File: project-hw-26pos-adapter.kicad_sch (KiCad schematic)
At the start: 3 parts, among them J1 SM04B-SRSS-TB(LF)(SN), J2 3220-26-0300-00, U1 Pink Panda v2.1.0

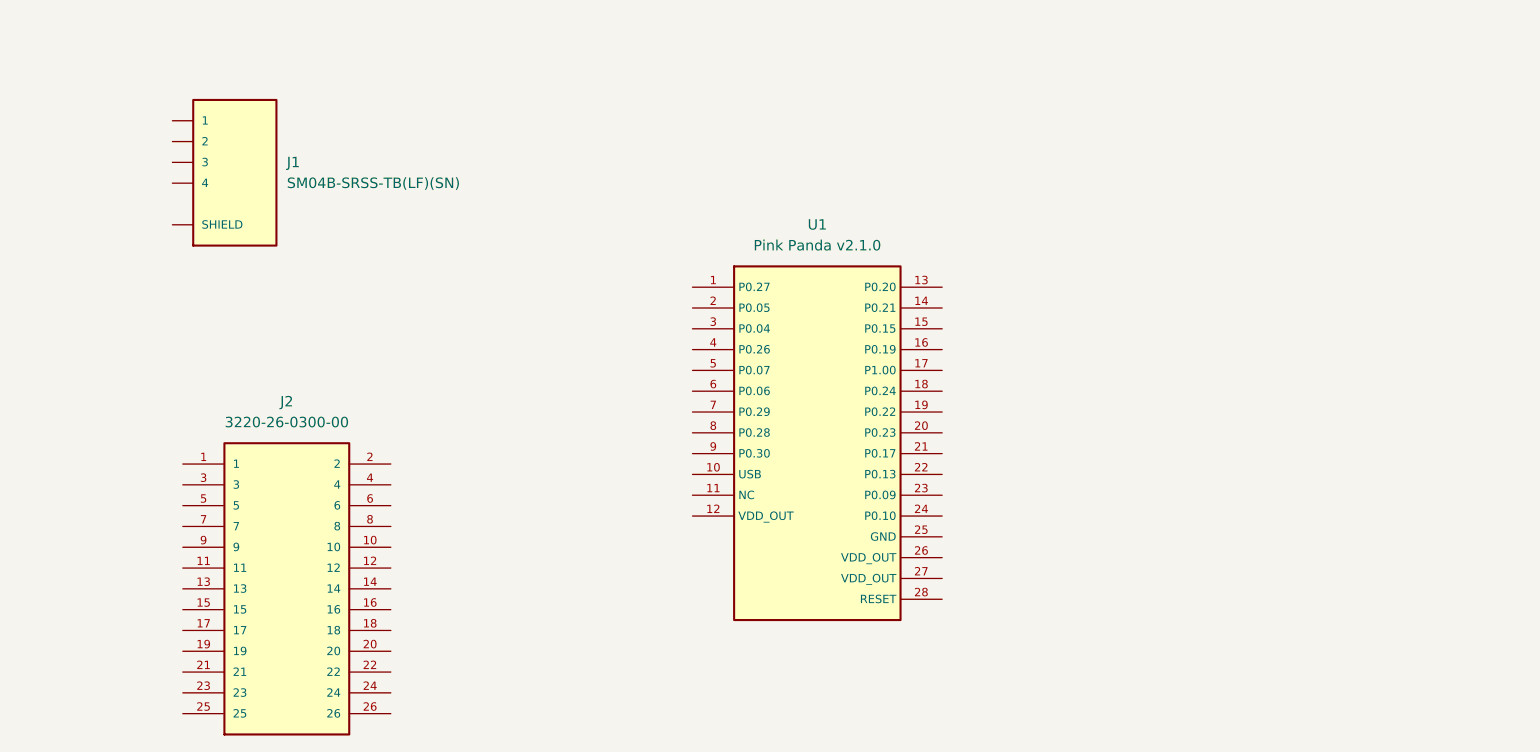
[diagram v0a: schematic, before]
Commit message: sch: add connections
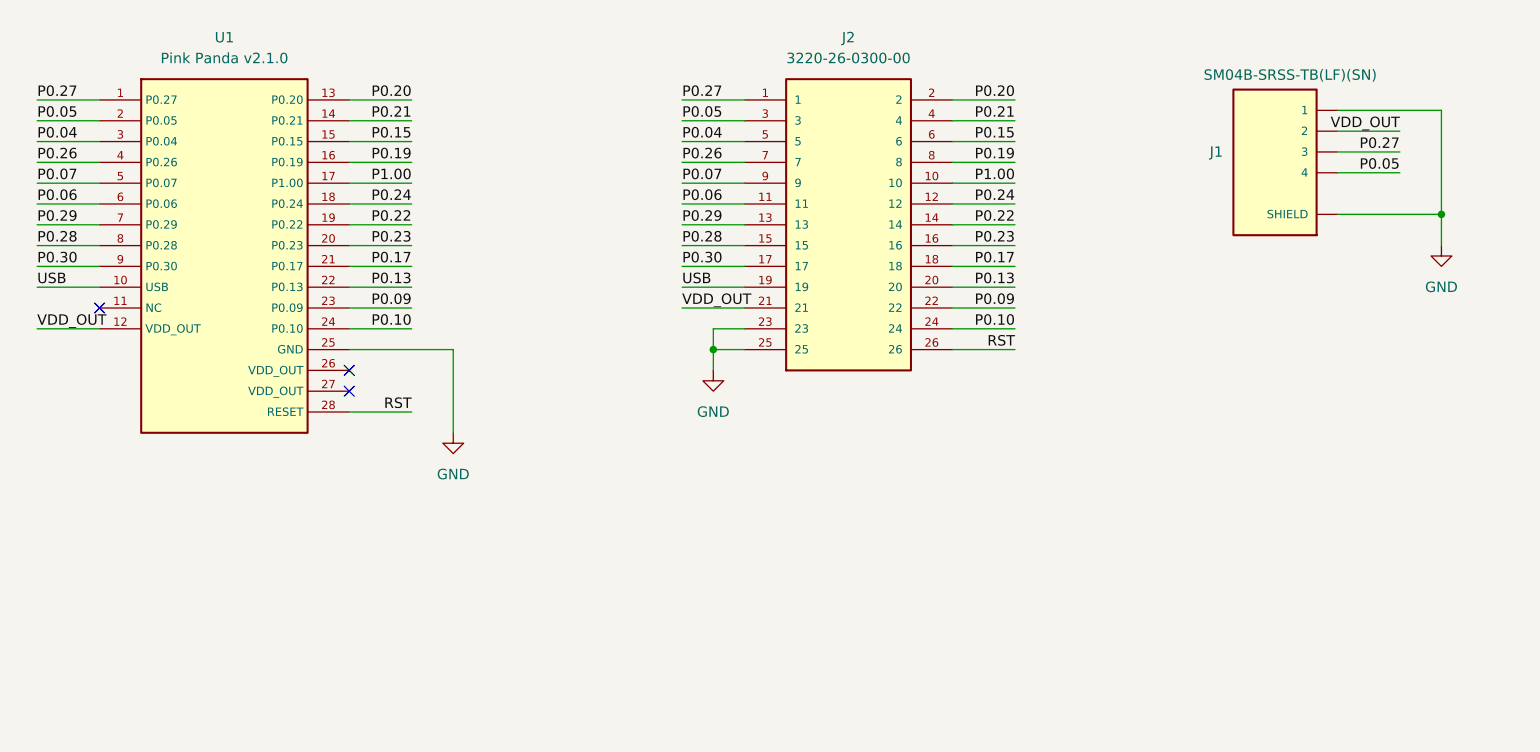
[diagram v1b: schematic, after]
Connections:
- net P0.27: now reaches U1.1 (P0.27)
- net P0.27: now also J1.3, J2.1
- net USB: now reaches U1.10 (USB)
- net USB: now also J2.19
- net VDD_OUT: now reaches U1.12 (VDD_OUT)
- net VDD_OUT: now also J1.2, J2.21
- net P0.20: now reaches U1.13 (P0.20)
- net P0.20: now also J2.2
- net P0.21: now reaches U1.14 (P0.21)
- net P0.21: now also J2.4
- net P0.15: now reaches U1.15 (P0.15)
- net P0.15: now also J2.6
- net P0.19: now reaches U1.16 (P0.19)
- net P0.19: now also J2.8
- net P1.00: now reaches U1.17 (P1.00)
- net P1.00: now also J2.10
- net P0.24: now reaches U1.18 (P0.24)
- net P0.24: now also J2.12
- net P0.22: now reaches U1.19 (P0.22)
- net P0.22: now also J2.14
- net P0.05: now reaches U1.2 (P0.05)
- net P0.05: now also J1.4, J2.3
- net P0.23: now reaches U1.20 (P0.23)
- net P0.23: now also J2.16
- net P0.17: now reaches U1.21 (P0.17)
- net P0.17: now also J2.18
- net P0.13: now reaches U1.22 (P0.13)
- net P0.13: now also J2.20
- net P0.09: now reaches U1.23 (P0.09)
- net P0.09: now also J2.22
- net P0.10: now reaches U1.24 (P0.10)
- net P0.10: now also J2.24
- net GND: now reaches U1.25 (GND)
- net GND: now also J1.1, J1.S1 (SHIELD), J1.S2 (SHIELD), J2.23, J2.25
- net RST: now reaches U1.28 (RESET)
- net RST: now also J2.26
- net P0.04: now reaches U1.3 (P0.04)
- net P0.04: now also J2.5
- net P0.26: now reaches U1.4 (P0.26)
- net P0.26: now also J2.7
- net P0.07: now reaches U1.5 (P0.07)
- net P0.07: now also J2.9
- net P0.06: now reaches U1.6 (P0.06)
- net P0.06: now also J2.11
- net P0.29: now reaches U1.7 (P0.29)
- net P0.29: now also J2.13
- net P0.28: now reaches U1.8 (P0.28)
- net P0.28: now also J2.15
- net P0.30: now reaches U1.9 (P0.30)
- net P0.30: now also J2.17
- no-connect marks 0 -> 3
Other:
- moved on the sheet: J1, J2, U1

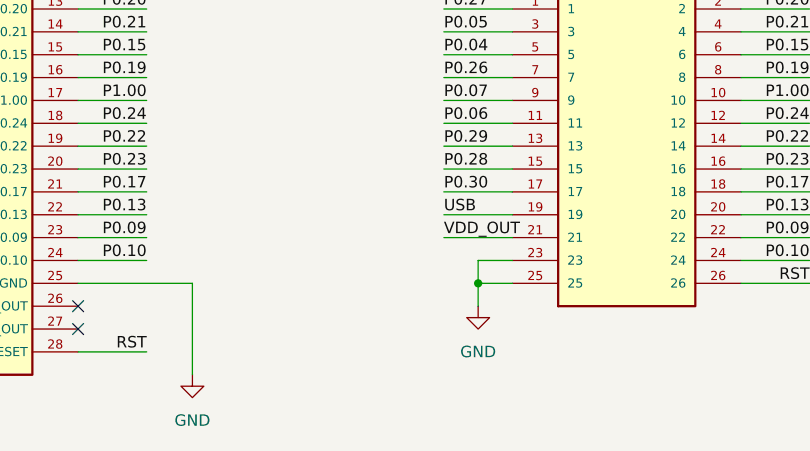
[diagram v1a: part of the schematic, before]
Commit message: pcb: first rough routing
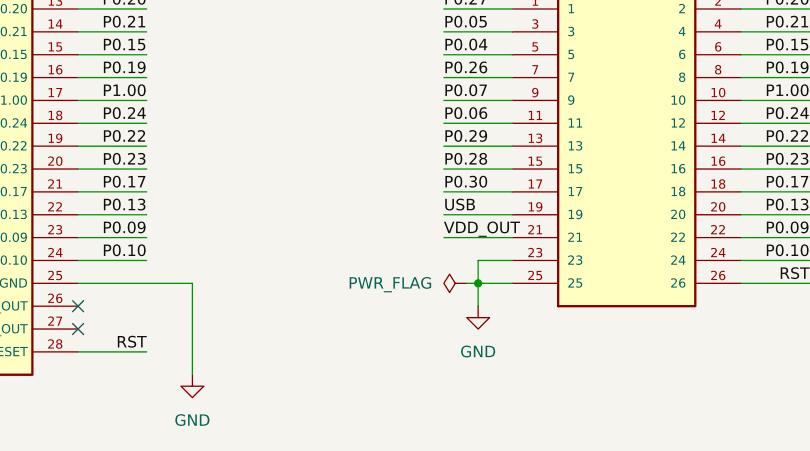
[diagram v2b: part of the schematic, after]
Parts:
- U1: footprint (none) -> pink_panda:pink_panda_SMD
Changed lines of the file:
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@@
+	(wire
+		(pts
+			(xy 105.41 58.42) (xy 106.68 58.42)
+		)
+		(stroke
+			(width 0)
+			(type default)
+		)
+	)
 	(wire
 		(pts
@@
 			)
 		)
-		(property "Footprint" ""
+		(property "Footprint" "pink_panda:pink_panda_SMD"
 			(at 46.99 34.29 0)
 			(effects
@@
 					(unit 1)
 				)
+			)
+		)
+	)
+	(symbol
+		(lib_id "power:PWR_FLAG")
+		(at 105.41 58.42 90)
+		(unit 1)
+		(exclude_from_sim no)
+		(in_bom yes)
+		(on_board yes)
+		(dnp no)
+		(fields_autoplaced yes)
+		(property "Reference" "#FLG01"
+			(at 103.505 58.42 0)
+			(effects
+				(font
+					(size 1.27 1.27)
+				)
+				(hide yes)
+			)
+		)
+		(property "Value" "PWR_FLAG"
+			(at 101.6 58.4199 90)
+			(effects
+				(font
+					(size 1.27 1.27)
+				)
+				(justify left)
+			)
+		)
+		(property "Footprint" ""
+			(at 105.41 58.42 0)
+			(effects
+				(font
+					(size 1.27 1.27)
+				)
+				(hide yes)
+			)
+		)
+		(property "Datasheet" "~"
+			(at 105.41 58.42 0)
+			(effects
+				(font
+					(size 1.27 1.27)
+				)
+				(hide yes)
+			)
+		)
+		(property "Description" "Special symbol for telling ERC where power comes from"
+			(at 105.41 58.42 0)
+			(effects
+				(font
+					(size 1.27 1.27)
+				)
+				(hide yes)
+			)
+		)
+		(pin "1"
+		)
+		(instances
+			(project ""
+				(path "/80c2b0ab-e7cb-44dd-baf2-a247c06b1c1b"
+					(reference "#FLG01")
+					(unit 1)
+				)

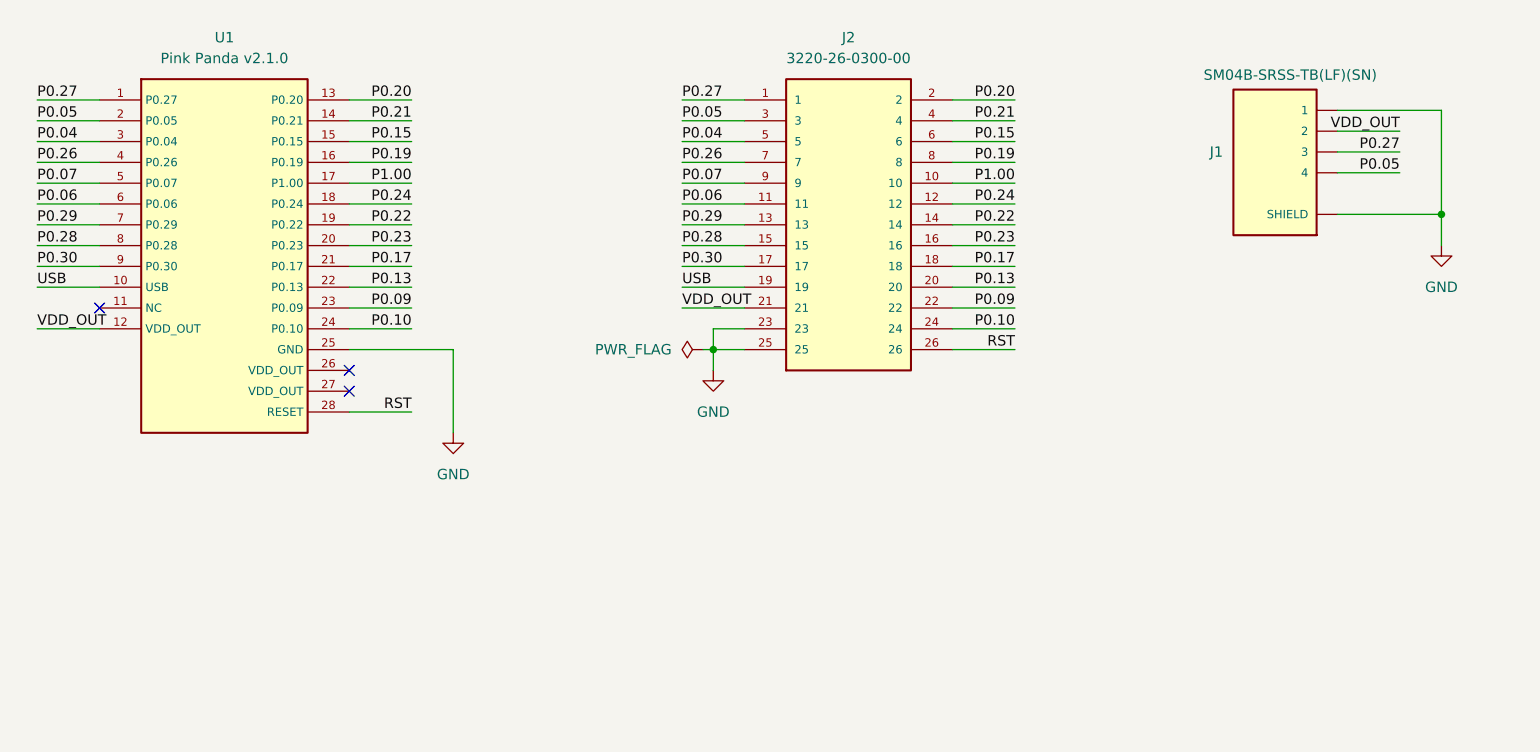
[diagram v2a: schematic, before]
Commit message: Add series resistors
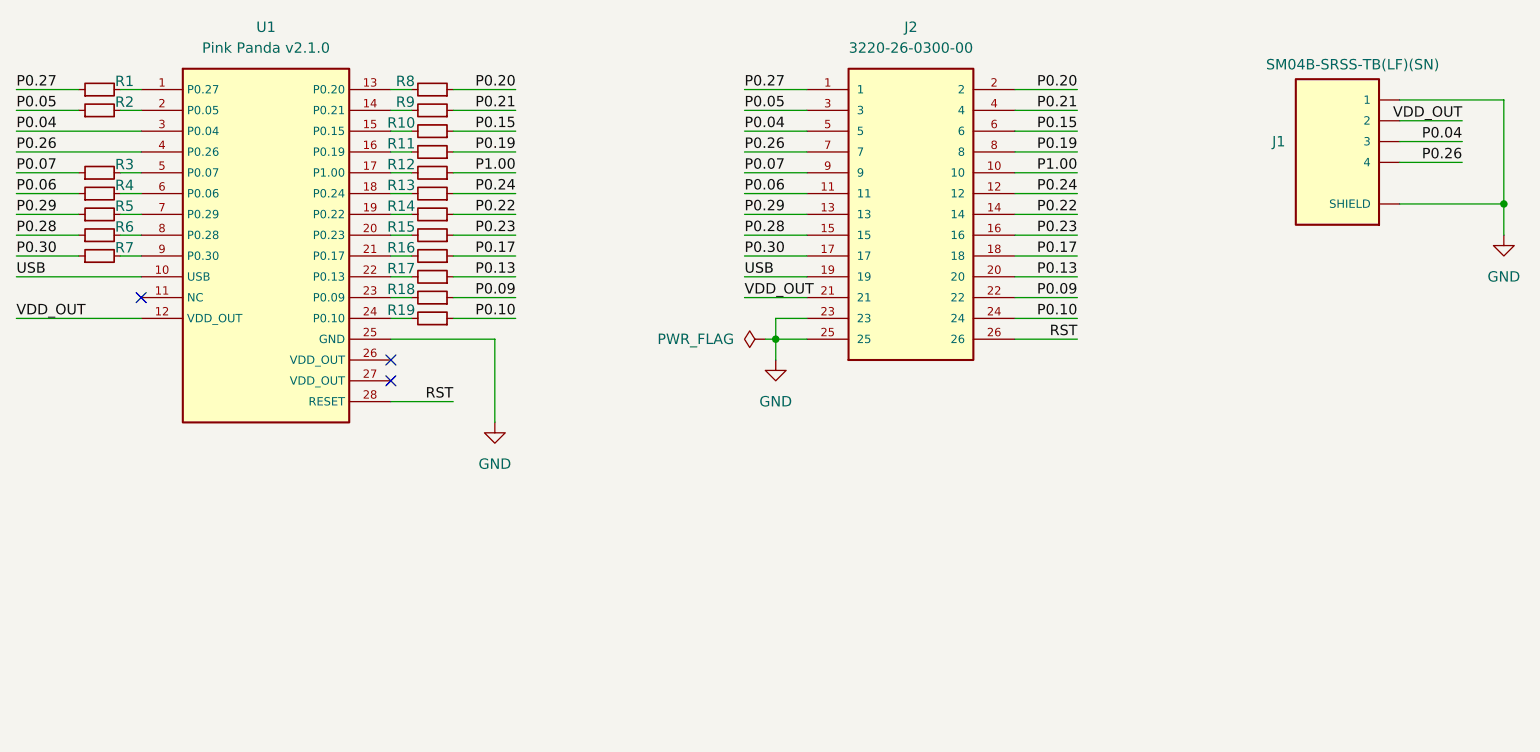
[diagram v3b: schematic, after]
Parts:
- added R1, R10, R11, R12, R13, R14, R15, R16, R17, R18, R19, R2, R3, R4, R5, R6, R7, R8, R9: R_Small, Resistor_SMD:R_0603_1608Metric, symbol Device:R_Small
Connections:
- net P0.04: now also J1.3
- net P0.05: now also R2.1; no longer J1.4, U1.2 (P0.05)
- net P0.06: now also R4.1; no longer U1.6 (P0.06)
- net P0.07: now also R3.1; no longer U1.5 (P0.07)
- net P0.09: now also R18.1; no longer U1.23 (P0.09)
- net P0.10: now also R19.1; no longer U1.24 (P0.10)
- net P0.13: now also R17.1; no longer U1.22 (P0.13)
- net P0.15: now also R10.1; no longer U1.15 (P0.15)
- net P0.17: now also R16.1; no longer U1.21 (P0.17)
- net P0.19: now also R11.1; no longer U1.16 (P0.19)
- net P0.20: now also R8.1; no longer U1.13 (P0.20)
- net P0.21: now also R9.1; no longer U1.14 (P0.21)
- net P0.22: now also R14.1; no longer U1.19 (P0.22)
- net P0.23: now also R15.1; no longer U1.20 (P0.23)
- net P0.24: now also R13.1; no longer U1.18 (P0.24)
- net P0.26: now also J1.4
- net P0.27: now also R1.1; no longer J1.3, U1.1 (P0.27)
- net P0.28: now also R6.1; no longer U1.8 (P0.28)
- net P0.29: now also R5.1; no longer U1.7 (P0.29)
- net P0.30: now also R7.1; no longer U1.9 (P0.30)
- net P1.00: now also R12.1; no longer U1.17 (P1.00)
- new net: R12.2, U1.17 (P1.00)
- new net: R3.2, U1.5 (P0.07)
- new net: R4.2, U1.6 (P0.06)
- new net: R11.2, U1.16 (P0.19)
- new net: R18.2, U1.23 (P0.09)
- new net: R1.2, U1.1 (P0.27)
- new net: R8.2, U1.13 (P0.20)
- new net: R9.2, U1.14 (P0.21)
- new net: R10.2, U1.15 (P0.15)
- new net: R13.2, U1.18 (P0.24)
- new net: R14.2, U1.19 (P0.22)
- new net: R2.2, U1.2 (P0.05)
- new net: R15.2, U1.20 (P0.23)
- new net: R16.2, U1.21 (P0.17)
- new net: R17.2, U1.22 (P0.13)
- new net: R19.2, U1.24 (P0.10)
- new net: R5.2, U1.7 (P0.29)
- new net: R6.2, U1.8 (P0.28)
- new net: R7.2, U1.9 (P0.30)
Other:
- moved on the sheet: J1, J2, U1

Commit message: Also add series resistors to SDA/SCL
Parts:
- added R20, R21: R_Small, Resistor_SMD:R_0603_1608Metric, symbol Device:R_Small
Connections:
- net P0.04: now also R20.1; no longer U1.3 (P0.04)
- net P0.26: now also R21.1; no longer U1.4 (P0.26)
- new net: R20.2, U1.3 (P0.04)
- new net: R21.2, U1.4 (P0.26)
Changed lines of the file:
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@@
+	(wire
+		(pts
+			(xy 21.59 31.75) (xy 29.21 31.75)
+		)
+		(stroke
+			(width 0)
+			(type default)
+		)
+	)
 	(wire
 		(pts
@@
 	(wire
 		(pts
+			(xy 34.29 31.75) (xy 36.83 31.75)
+		)
+		(stroke
+			(width 0)
+			(type default)
+		)
+	)
+	(wire
+		(pts
 			(xy 143.51 54.61) (xy 151.13 54.61)
 		)
@@
 	(wire
 		(pts
-			(xy 21.59 31.75) (xy 36.83 31.75)
-		)
-		(stroke
-			(width 0)
-			(type default)
-		)
-	)
-	(wire
-		(pts
 			(xy 114.3 54.61) (xy 118.11 54.61)
 		)
@@
 	(wire
 		(pts
-			(xy 21.59 34.29) (xy 36.83 34.29)
+			(xy 21.59 34.29) (xy 29.21 34.29)
 		)
 		(stroke
@@
 		(pts
 			(xy 190.5 27.94) (xy 203.2 27.94)
+		)
+		(stroke
+			(width 0)
+			(type default)
+		)
+	)
+	(wire
+		(pts
+			(xy 34.29 34.29) (xy 36.83 34.29)
 		)
 		(stroke
@@
 	)
 	(symbol
+		(lib_id "Device:R_Small")
+		(at 31.75 31.75 90)
+		(unit 1)
+		(exclude_from_sim no)
+		(in_bom yes)
+		(on_board yes)
+		(dnp no)
+		(property "Reference" "R20"
+			(at 35.56 30.734 90)
+			(effects
+				(font
+					(size 1.27 1.27)
+				)
+			)
+		)
+		(property "Value" "R_Small"
+			(at 33.0199 29.21 0)
+			(effects
+				(font
+					(size 1.27 1.27)
+				)
+				(justify left)
+				(hide yes)
+			)
+		)
+		(property "Footprint" "Resistor_SMD:R_0603_1608Metric"
+			(at 31.75 31.75 0)
+			(effects
+				(font
+					(size 1.27 1.27)
+				)
+				(hide yes)
+			)
+		)
+		(property "Datasheet" "~"
+			(at 31.75 31.75 0)
+			(effects
+				(font
+					(size 1.27 1.27)
+				)
+				(hide yes)
+			)
+		)
+		(property "Description" "Resistor, small symbol"
+			(at 31.75 31.75 0)
+			(effects
+				(font
+					(size 1.27 1.27)
+				)
+				(hide yes)
+			)
+		)
+		(pin "1"
+		)
+		(pin "2"
+		)
+		(instances
+			(project "project-hw-26pos-adapter"
+				(path "/80c2b0ab-e7cb-44dd-baf2-a247c06b1c1b"
+					(reference "R20")
+					(unit 1)
+				)
+			)
+		)
+	)
+	(symbol
 		(lib_id "power:PWR_FLAG")
 		(at 113.03 57.15 90)
@@
 					(unit 1)
 				)
+			)
+		)
+	)
+	(symbol
+		(lib_id "Device:R_Small")
+		(at 31.75 34.29 90)
+		(unit 1)
+		(exclude_from_sim no)
+		(in_bom yes)
+		(on_board yes)
+		(dnp no)
+		(property "Reference" "R21"
+			(at 35.56 33.274 90)
+			(effects
+				(font
+					(size 1.27 1.27)
+				)
+			)
+		)
+		(property "Value" "R_Small"
+			(at 33.0199 31.75 0)
+			(effects
+				(font
+					(size 1.27 1.27)
+				)
+				(justify left)
+				(hide yes)
+			)
+		)
+		(property "Footprint" "Resistor_SMD:R_0603_1608Metric"
+			(at 31.75 34.29 0)
+			(effects
+				(font
+					(size 1.27 1.27)
+				)
+				(hide yes)
+			)
+		)
+		(property "Datasheet" "~"
+			(at 31.75 34.29 0)
+			(effects
+				(font
+					(size 1.27 1.27)
+				)
+				(hide yes)
+			)
+		)
+		(property "Description" "Resistor, small symbol"
+			(at 31.75 34.29 0)
+			(effects
+				(font
+					(size 1.27 1.27)
+				)
+				(hide yes)
+			)
+		)
+		(pin "1"
+		)
+		(pin "2"
+		)
+		(instances
+			(project "project-hw-26pos-adapter"
+				(path "/80c2b0ab-e7cb-44dd-baf2-a247c06b1c1b"
+					(reference "R21")
+					(unit 1)
+				)
